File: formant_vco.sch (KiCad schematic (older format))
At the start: 76 parts, among them J1 JACK_2P, J2 JACK_2P, J3 JACK_2P, J4 CONN_01X03, J5 JACK_2P, Q1 BC850, Q2 BC850, Q3 BC850, Q4 BC850, Q5 BC850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

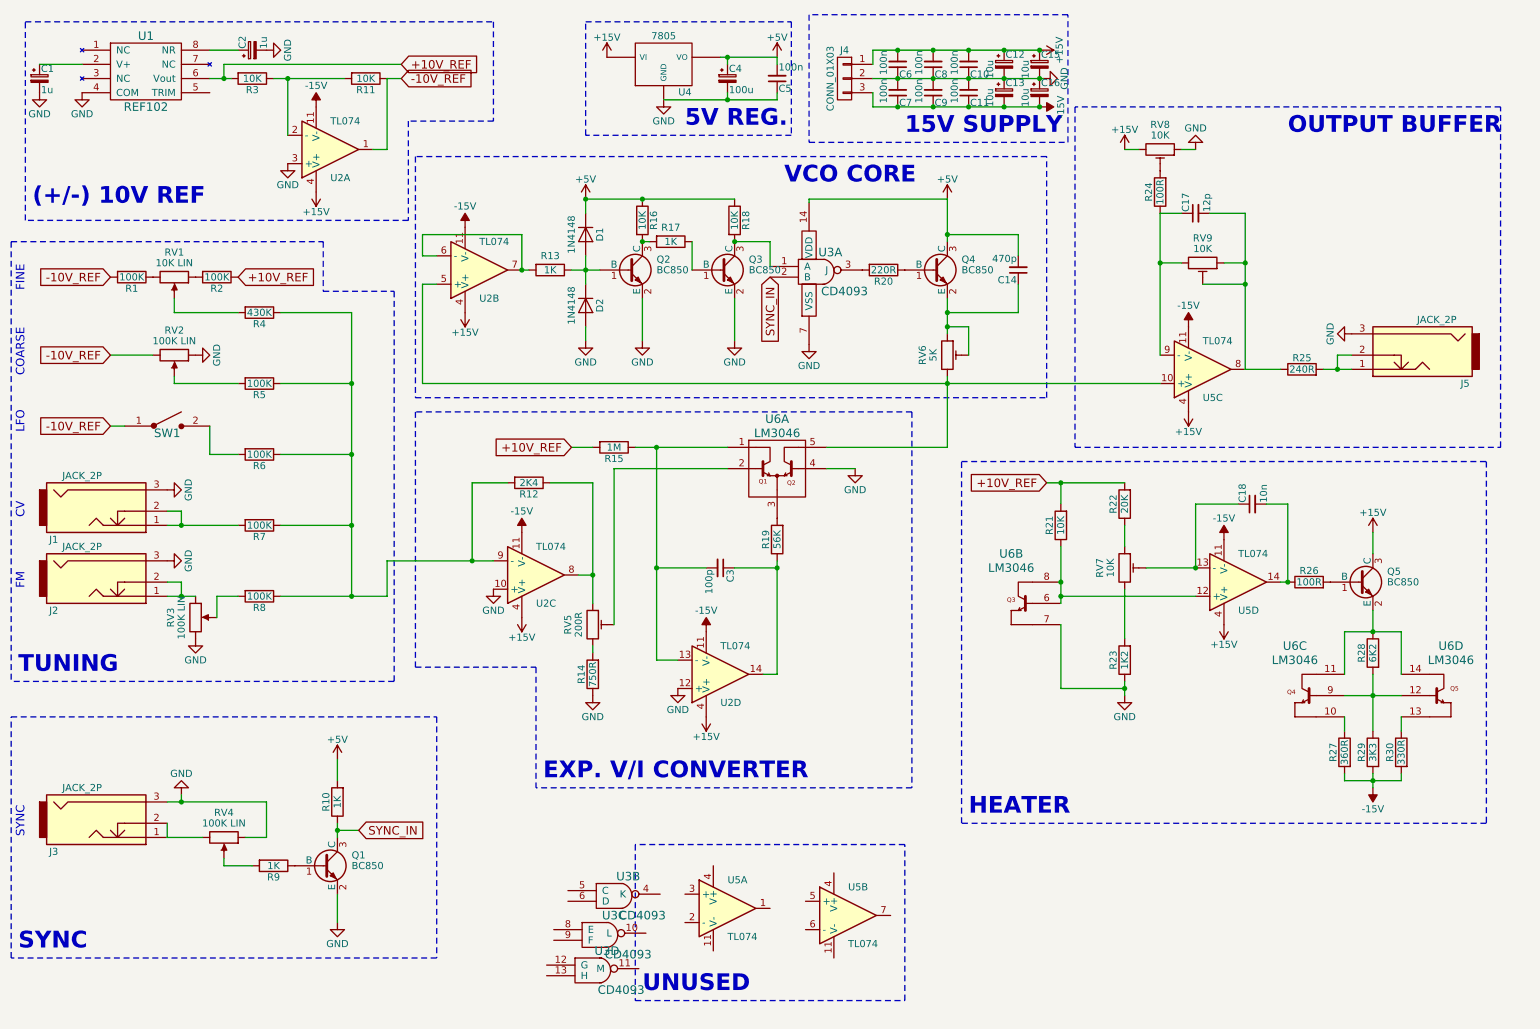
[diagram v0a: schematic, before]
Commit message: Add eurorack synth power header
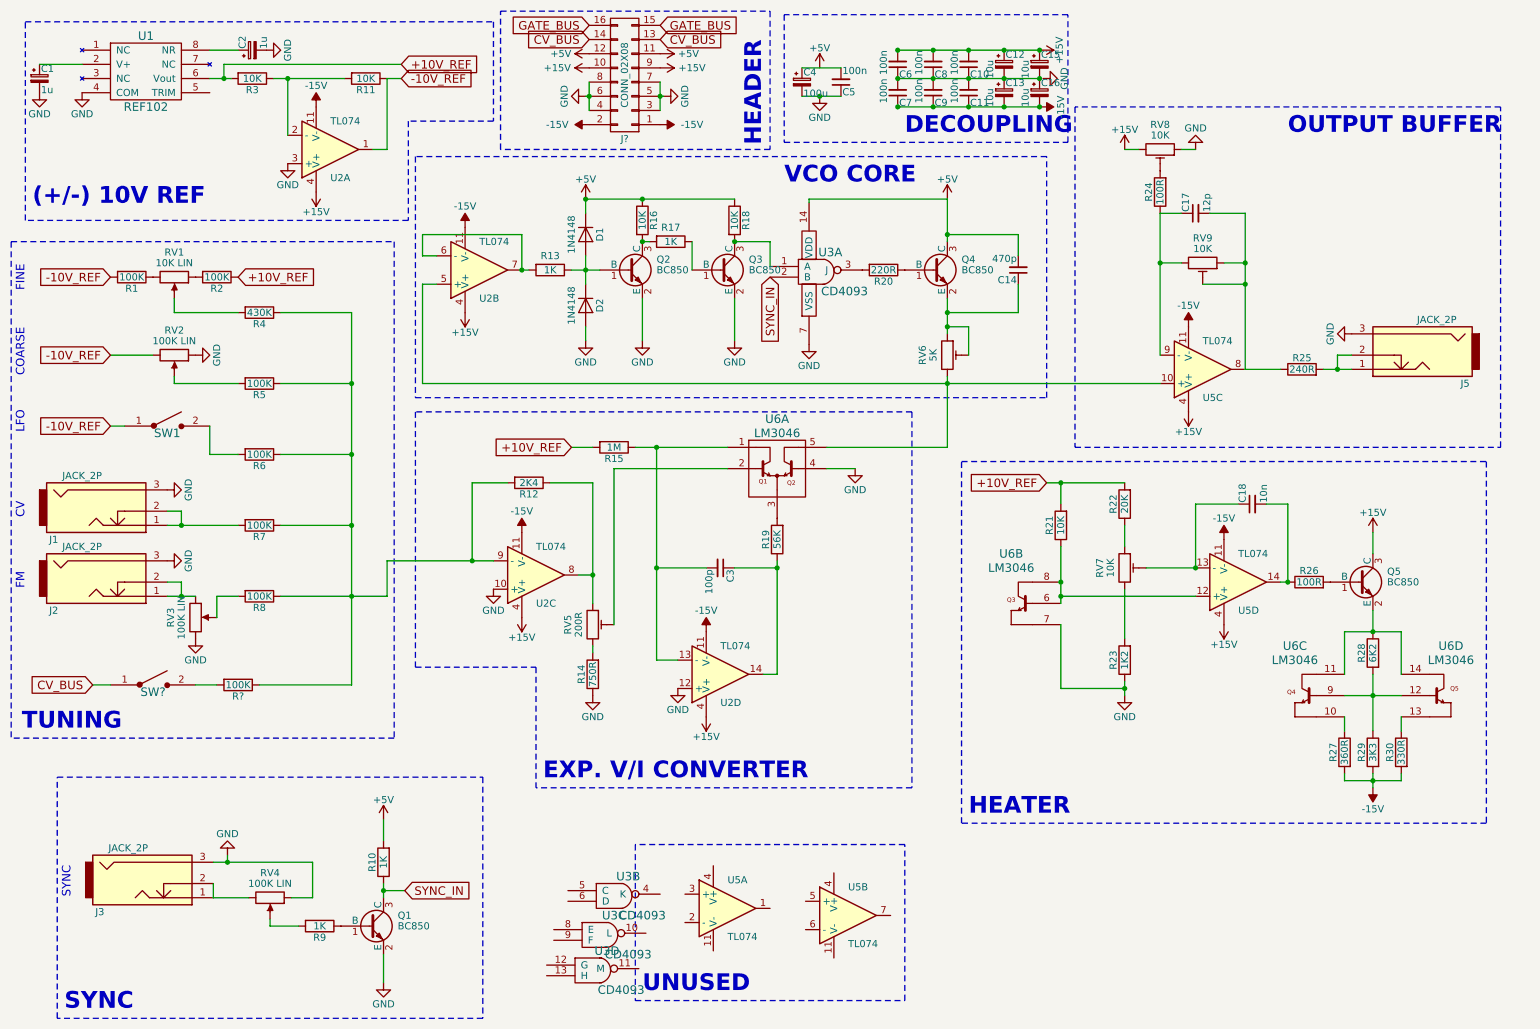
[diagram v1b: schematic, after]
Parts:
- removed J4: CONN_01X03, Pin_Headers:Pin_Header_Straight_1x03_Pitch2.54mm, symbol CONN_01X03
- removed U4: 7805, symbol 7805
- added J?: CONN_02X08, symbol CONN_02X08
- added R?: 100K, Resistors_SMD:R_0603, symbol R
- added SW?: SWITCH_SPST, Pin_Headers:Pin_Header_Straight_2x01_Pitch2.54mm, symbol SWITCH_SPST
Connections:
- net +15V: now also J?.10 (P10), J?.9 (P9)
- net +5V: now also J?.11 (P11), J?.12 (P12); no longer C4.1, C5.2
- net -15V: now also J?.1 (P1), J?.2 (P2)
- net GND: now also J?.3 (P3), J?.4 (P4), J?.5 (P5), J?.6 (P6), J?.7 (P7), J?.8 (P8); no longer C10.1, C11.2, C12.2, C13.1, C15.2, C16.1, C6.1, C7.2, C8.1, C9.2
- net at R12.2, R4.1, R5.1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: now also R?.1
- new net: C4.1, C5.2
- new net: C10.1, C11.2, C12.2, C13.1, C15.2, C16.1, C6.1, C7.2, C8.1, C9.2
- new net: R?.2, SW?.2
- new net CV_BUS: J?.13 (P13), J?.14 (P14), SW?.1
- new net GATE_BUS: J?.15 (P15), J?.16 (P16)
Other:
- note added: "DECOUPLING"
- note added: "HEADER"
- note removed: "15V SUPPLY"
- note removed: "5V REG."
- moved on the sheet: C4, C5, J3, Q1, R10, R9, RV4

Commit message: Add output indicator LEDS
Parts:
- added D? (x2): LED, symbol LED
- added R?: 1K, Resistors_SMD:R_0603, symbol R
- gave numbers to parts that had none: 3
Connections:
- net +15V: now also U5.4 (V+)
- net -15V: now also U5.11 (V-)
- net GND: now also D?.1 (K), D?.2 (A)
- net at C17.2, R25.1, RV9.1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: now also U5.3 (+)
- net at U5.1: now also U5.2 (-), R?.2
- new net: D?.1 (K), D?.2 (A), R?.1
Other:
- moved on the sheet: U5A
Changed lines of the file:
@@
 $EndComp
 $Comp
-L -15V #PWR26
+L -15V #PWR32
 U 1 1 59607E23
 P 5400 4900
-F 0 "#PWR26" H 5400 5000 50  0001 C CNN
+F 0 "#PWR32" H 5400 5000 50  0001 C CNN
 F 1 "-15V" H 5400 5050 50  0000 C CNN
 F 2 "" H 5400 4900 50  0001 C CNN
@@
 L TL074 U5
 U 1 1 59630B3B
-P 5550 6850
-F 0 "U5" H 5550 7050 50  0000 L CNN
-F 1 "TL074" H 5550 6650 50  0000 L CNN
-F 2 "Housings_SOIC:SOIC-14_3.9x8.7mm_Pitch1.27mm" H 5500 6950 50  0001 C CNN
-F 3 "" H 5600 7050 50  0001 C CNN
-	1    5550 6850
+P 9775 1925
+F 0 "U5" H 9775 2125 50  0000 L CNN
+F 1 "TL074" H 9775 1725 50  0000 L CNN
+F 2 "Housings_SOIC:SOIC-14_3.9x8.7mm_Pitch1.27mm" H 9725 2025 50  0001 C CNN
+F 3 "" H 9825 2125 50  0001 C CNN
+	1    9775 1925
 	1    0    0    -1
 $EndComp
@@
 $EndComp
 $Comp
-L -15V #PWR38
+L -15V #PWR45
 U 1 1 596352FD
 P 8800 2750
-F 0 "#PWR38" H 8800 2850 50  0001 C CNN
+F 0 "#PWR45" H 8800 2850 50  0001 C CNN
 F 1 "-15V" H 8800 2900 50  0000 C CNN
 F 2 "" H 8800 2750 50  0001 C CNN
@@
 $EndComp
 $Comp
-L GND #PWR030
+L GND #PWR029
 U 1 1 5964540C
 P 6200 1125
-F 0 "#PWR030" H 6200 875 50  0001 C CNN
+F 0 "#PWR029" H 6200 875 50  0001 C CNN
 F 1 "GND" H 6200 975 50  0000 C CNN
 F 2 "" H 6200 1125 50  0001 C CNN
@@
 $EndComp
 $Comp
-L +5V #PWR031
+L +5V #PWR030
 U 1 1 596454C2
 P 6200 925
-F 0 "#PWR031" H 6200 775 50  0001 C CNN
+F 0 "#PWR030" H 6200 775 50  0001 C CNN
 F 1 "+5V" H 6200 1065 50  0000 C CNN
 F 2 "" H 6200 925 50  0001 C CNN
@@
 SYNC
 $Comp
-L -15V #PWR41
+L -15V #PWR48
 U 1 1 5961BD3A
 P 9050 4250
-F 0 "#PWR41" H 9050 4350 50  0001 C CNN
+F 0 "#PWR48" H 9050 4350 50  0001 C CNN
 F 1 "-15V" H 9050 4400 50  0000 C CNN
 F 2 "" H 9050 4250 50  0001 C CNN
@@
 $EndComp
 $Comp
-L +15V #PWR032
+L +15V #PWR031
 U 1 1 5961BEAB
 P 9050 4850
-F 0 "#PWR032" H 9050 4700 50  0001 C CNN
+F 0 "#PWR031" H 9050 4700 50  0001 C CNN
 F 1 "+15V" H 9050 4990 50  0000 C CNN
 F 2 "" H 9050 4850 50  0001 C CNN
@@
 $EndComp
 $Comp
-L GND #PWR033
+L GND #PWR032
 U 1 1 596225D4
 P 8350 5350
-F 0 "#PWR033" H 8350 5100 50  0001 C CNN
+F 0 "#PWR032" H 8350 5100 50  0001 C CNN
 F 1 "GND" H 8350 5200 50  0000 C CNN
 F 2 "" H 8350 5350 50  0001 C CNN
@@
 $EndComp
 $Comp
-L +15V #PWR034
+L +15V #PWR033
 U 1 1 59625139
 P 10100 4200
-F 0 "#PWR034" H 10100 4050 50  0001 C CNN
+F 0 "#PWR033" H 10100 4050 50  0001 C CNN
 F 1 "+15V" H 10100 4340 50  0000 C CNN
 F 2 "" H 10100 4200 50  0001 C CNN
@@
 $EndComp
 $Comp
-L -15V #PWR45
+L -15V #PWR52
 U 1 1 59626FF8
 P 10100 6000
-F 0 "#PWR45" H 10100 6100 50  0001 C CNN
+F 0 "#PWR52" H 10100 6100 50  0001 C CNN
 F 1 "-15V" H 10100 6150 50  0000 C CNN
 F 2 "" H 10100 6000 50  0001 C CNN
@@
 EXP. V/I CONVERTER
 $Comp
-L -15V #PWR34
+L -15V #PWR41
 U 1 1 59652164
 P 7750 1200
-F 0 "#PWR34" H 7750 1300 50  0001 C CNN
+F 0 "#PWR41" H 7750 1300 50  0001 C CNN
 F 1 "-15V" H 7750 1350 50  0000 C CNN
 F 2 "" H 7750 1200 50  0001 C CNN
@@
 $EndComp
 $Comp
-L +15V #PWR035
+L +15V #PWR034
 U 1 1 59652247
 P 7750 800
-F 0 "#PWR035" H 7750 650 50  0001 C CNN
+F 0 "#PWR034" H 7750 650 50  0001 C CNN
 F 1 "+15V" H 7750 940 50  0000 C CNN
 F 2 "" H 7750 800 50  0001 C CNN
@@
 $EndComp
 $Comp
-L GND #PWR036
+L GND #PWR035
 U 1 1 5965232A
 P 7775 1000
-F 0 "#PWR036" H 7775 750 50  0001 C CNN
+F 0 "#PWR035" H 7775 750 50  0001 C CNN
 F 1 "GND" H 7775 850 50  0000 C CNN
 F 2 "" H 7775 1000 50  0001 C CNN
@@
 $EndComp
 $Comp
-L GND #PWR037
+L GND #PWR036
 U 1 1 59628271
 P 6125 2875
-F 0 "#PWR037" H 6125 2625 50  0001 C CNN
+F 0 "#PWR036" H 6125 2625 50  0001 C CNN
 F 1 "GND" H 6125 2725 50  0000 C CNN
 F 2 "" H 6125 2875 50  0001 C CNN
@@
 	5950 550  5950 1450
 $Comp
-L CONN_02X08 J?
+L CONN_02X08 J4
 U 1 1 5969AA3B
 P 4825 975
-F 0 "J?" H 4825 1425 50  0000 C CNN
+F 0 "J4" H 4825 1425 50  0000 C CNN
 F 1 "CONN_02X08" V 4825 975 50  0000 C CNN
 F 2 "" H 4825 -225 50  0001 C CNN
@@
 $EndComp
 $Comp
-L -15V #PWR?
+L -15V #PWR29
 U 1 1 5969B96D
 P 5075 1325
-F 0 "#PWR?" H 5075 1425 50  0001 C CNN
+F 0 "#PWR29" H 5075 1425 50  0001 C CNN
 F 1 "-15V" V 5075 1550 50  0000 C CNN
 F 2 "" H 5075 1325 50  0001 C CNN
@@
 $EndComp
 $Comp
-L +5V #PWR?
+L +5V #PWR037
 U 1 1 5969D054
 P 5075 825
-F 0 "#PWR?" H 5075 675 50  0001 C CNN
+F 0 "#PWR037" H 5075 675 50  0001 C CNN
 F 1 "+5V" V 5075 1025 50  0000 C CNN
 F 2 "" H 5075 825 50  0001 C CNN
@@
 $EndComp
 $Comp
-L GND #PWR?
+L GND #PWR038
 U 1 1 596A0073
 P 5100 1125
-F 0 "#PWR?" H 5100 875 50  0001 C CNN
+F 0 "#PWR038" H 5100 875 50  0001 C CNN
 F 1 "GND" H 5100 975 50  0000 C CNN
 F 2 "" H 5100 1125 50  0001 C CNN
@@
 GATE_BUS
 $Comp
-L -15V #PWR?
+L -15V #PWR24
 U 1 1 596A3A13
 P 4575 1325
-F 0 "#PWR?" H 4575 1425 50  0001 C CNN
+F 0 "#PWR24" H 4575 1425 50  0001 C CNN
 F 1 "-15V" V 4575 1550 50  0000 C CNN
 F 2 "" H 4575 1325 50  0001 C CNN
@@
 $EndComp
 $Comp
-L GND #PWR?
+L GND #PWR039
 U 1 1 596A3B23
 P 4550 1125
-F 0 "#PWR?" H 4550 875 50  0001 C CNN
+F 0 "#PWR039" H 4550 875 50  0001 C CNN
 F 1 "GND" H 4550 975 50  0000 C CNN
 F 2 "" H 4550 1125 50  0001 C CNN
@@
 $EndComp
 $Comp
-L +5V #PWR?
+L +5V #PWR040
 U 1 1 596A3D43
 P 4575 825
-F 0 "#PWR?" H 4575 675 50  0001 C CNN
+F 0 "#PWR040" H 4575 675 50  0001 C CNN
 F 1 "+5V" V 4575 1025 50  0000 C CNN
 F 2 "" H 4575 825 50  0001 C CNN
@@
 	4550 1125 4575 1125
 $Comp
-L R R?
+L R R31
 U 1 1 596AC73A
 P 2100 5275
-F 0 "R?" V 2180 5275 50  0000 C CNN
+F 0 "R31" V 2180 5275 50  0000 C CNN
 F 1 "100K" V 2100 5275 50  0000 C CNN
 F 2 "Resistors_SMD:R_0603" V 2030 5275 50  0001 C CNN
@@
 	3200 5650 500  5650
 $Comp
-L SWITCH_SPST SW?
+L SWITCH_SPST SW2
 U 1 1 596B4A56
 P 1500 5275
-F 0 "SW?" H 1500 5225 60  0000 C CNN
+F 0 "SW2" H 1500 5225 60  0000 C CNN
 F 1 "SWITCH_SPST" H 1550 5525 60  0001 C CNN
 F 2 "Pin_Headers:Pin_Header_Straight_2x01_Pitch2.54mm" H 1500 5275 60  0001 C CNN
@@
 	1200 5275 1075 5275
 $Comp
-L +15V #PWR?
+L +15V #PWR041
 U 1 1 5969C6B9
 P 5075 925
-F 0 "#PWR?" H 5075 775 50  0001 C CNN
+F 0 "#PWR041" H 5075 775 50  0001 C CNN
 F 1 "+15V" V 5075 1150 50  0000 C CNN
 F 2 "" H 5075 925 50  0001 C CNN
@@
 $EndComp
 $Comp
-L +15V #PWR?
+L +15V #PWR042
 U 1 1 596A3C33
 P 4575 925
-F 0 "#PWR?" H 4575 775 50  0001 C CNN
+F 0 "#PWR042" H 4575 775 50  0001 C CNN
 F 1 "+15V" V 4575 1150 50  0000 C CNN
 F 2 "" H 4575 925 50  0001 C CNN
@@
 	0    -1   -1   0
 $EndComp
+$Comp
+L -15V #PWR?
+U 1 1 5969C174
+P 9675 2225
+F 0 "#PWR?" H 9675 2325 50  0001 C CNN
+F 1 "-15V" H 9675 2375 50  0000 C CNN
+F 2 "" H 9675 2225 50  0001 C CNN
+F 3 "" H 9675 2225 50  0001 C CNN
+	1    9675 2225
+	-1   0    0    1
+$EndComp
+$Comp
+L +15V #PWR?
+U 1 1 5969C4B0
+P 9675 1625
+F 0 "#PWR?" H 9675 1475 50  0001 C CNN
+F 1 "+15V" H 9675 1765 50  0000 C CNN
+F 2 "" H 9675 1625 50  0001 C CNN
+F 3 "" H 9675 1625 50  0001 C CNN
+	1    9675 1625
+	-1   0    0    -1
+$EndComp
+Wire Wire Line
+	9475 2025 9475 2500
+Wire Wire Line
+	9475 2500 10125 2500
+Wire Wire Line
+	10125 2500 10125 1925
+Wire Wire Line
+	10125 1925 10075 1925
+Wire Wire Line
+	9350 1825 9350 3050
+Connection ~ 9350 3050
+$Comp
+L R R?
+U 1 1 5969C9D5
+P 10275 1925
+F 0 "R?" V 10175 1925 50  0000 C CNN
+F 1 "1K" V 10275 1925 50  0000 C CNN
+F 2 "Resistors_SMD:R_0603" V 10205 1925 50  0001 C CNN
+F 3 "" H 10275 1925 50  0001 C CNN
+	1    10275 1925
+	0    1    1    0
+$EndComp
+Connection ~ 10125 1925
+$Comp
+L LED D?
+U 1 1 5969DEA1
+P 10525 2075
+F 0 "D?" H 10525 2175 50  0000 C CNN
+F 1 "LED" H 10525 1975 50  0000 C CNN
+F 2 "" H 10525 2075 50  0001 C CNN
+F 3 "" H 10525 2075 50  0001 C CNN
+	1    10525 2075
+	0    -1   -1   0
+$EndComp
+$Comp
+L GND #PWR?
+U 1 1 5969E2E1
+P 10525 2225
+F 0 "#PWR?" H 10525 1975 50  0001 C CNN
+F 1 "GND" H 10525 2075 50  0000 C CNN
+F 2 "" H 10525 2225 50  0001 C CNN
+F 3 "" H 10525 2225 50  0001 C CNN
+	1    10525 2225
+	1    0    0    -1
+$EndComp
+Wire Wire Line
+	10425 1925 10850 1925
+$Comp
+L LED D?
+U 1 1 596A27BF
+P 10850 2075
+F 0 "D?" H 10850 2175 50  0000 C CNN
+F 1 "LED" H 10850 1975 50  0000 C CNN
+F 2 "" H 10850 2075 50  0001 C CNN
+F 3 "" H 10850 2075 50  0001 C CNN
+	1    10850 2075
+	0    1    1    0
+$EndComp
+$Comp
+L GND #PWR?
+U 1 1 596A2901
+P 10850 2225
+F 0 "#PWR?" H 10850 1975 50  0001 C CNN
+F 1 "GND" H 10850 2075 50  0000 C CNN
+F 2 "" H 10850 2225 50  0001 C CNN
+F 3 "" H 10850 2225 50  0001 C CNN
+	1    10850 2225
+	1    0    0    -1
+$EndComp
+Connection ~ 10525 1925
+Wire Wire Line
+	9475 1825 9350 1825
 $EndSCHEMATC
